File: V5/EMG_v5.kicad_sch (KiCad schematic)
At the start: 1 part, among them U501 DSTK22807_ESP32H2_SuperMini_M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

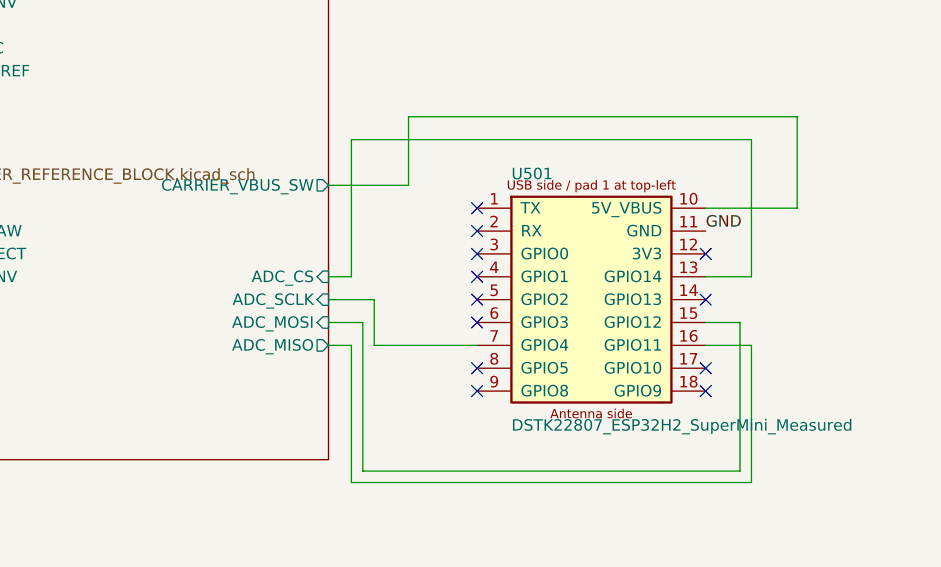
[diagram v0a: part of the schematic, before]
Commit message: add unequal-power spi isolation
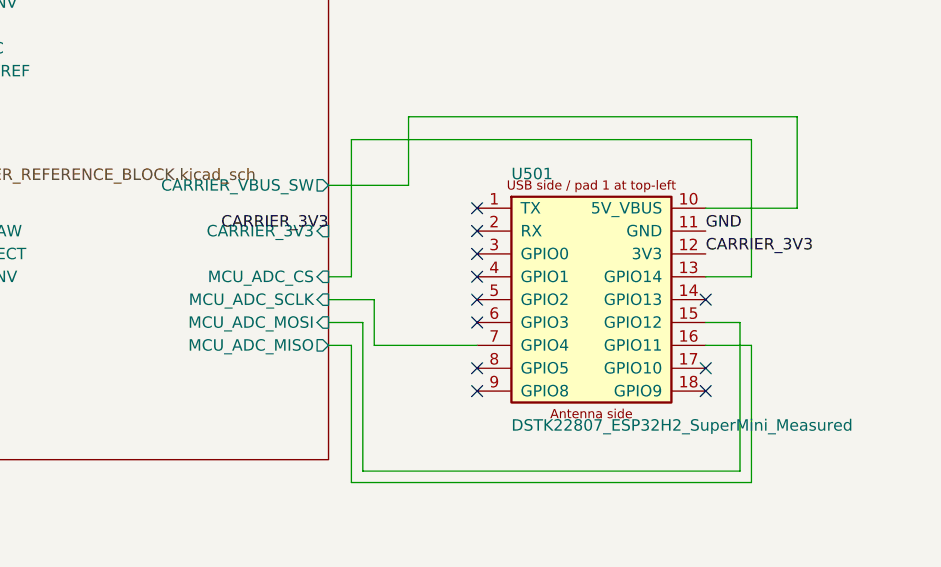
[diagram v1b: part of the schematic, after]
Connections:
- net CARRIER_3V3: now reaches U501.12 (3V3)
- net POWER_REFERENCE_BLOCK/ADC_CS renamed POWER_REFERENCE_BLOCK/MCU_ADC_CS
- net POWER_REFERENCE_BLOCK/ADC_MISO renamed POWER_REFERENCE_BLOCK/MCU_ADC_MISO
- net POWER_REFERENCE_BLOCK/ADC_MOSI renamed POWER_REFERENCE_BLOCK/MCU_ADC_MOSI
- net POWER_REFERENCE_BLOCK/ADC_SCLK renamed POWER_REFERENCE_BLOCK/MCU_ADC_SCLK
- no-connect marks 12 -> 11
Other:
- sheet POWER_REFERENCE_BLOCK ports: added CARRIER_3V3, MCU_ADC_CS, MCU_ADC_MISO, MCU_ADC_MOSI, MCU_ADC_SCLK; removed ADC_CS, ADC_MISO, ADC_MOSI, ADC_SCLK
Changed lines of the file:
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@@
 		(at 185.42 74.93)
 	)
-	(no_connect
-		(at 210.82 59.69)
+	(label "CARRIER_3V3"
+		(at 210.82 59.69 0)
+		(effects (font (size 1.27 1.27)) (justify left bottom))
+	)
+	(label "CARRIER_3V3"
+		(at 168.91 57.15 180)
+		(effects (font (size 1.27 1.27)) (justify right bottom))
 	)
 	(no_connect
@@
 			)
 		)
-		(pin "ADC_MISO" output
+		(pin "CARRIER_3V3" input
+			(at 168.91 57.15 0)
+			(effects (font (size 1.27 1.27)) (justify right))
+		)
+		(pin "MCU_ADC_MISO" output
 			(at 168.91 69.85 0)
 			(effects
@@
 			)
 		)
-		(pin "ADC_MOSI" input
+		(pin "MCU_ADC_MOSI" input
 			(at 168.91 67.31 0)
 			(effects
@@
 			)
 		)
-		(pin "ADC_SCLK" input
+		(pin "MCU_ADC_SCLK" input
 			(at 168.91 64.77 0)
 			(effects
@@
 			)
 		)
-		(pin "ADC_CS" input
+		(pin "MCU_ADC_CS" input
 			(at 168.91 62.23 0)
 			(effects

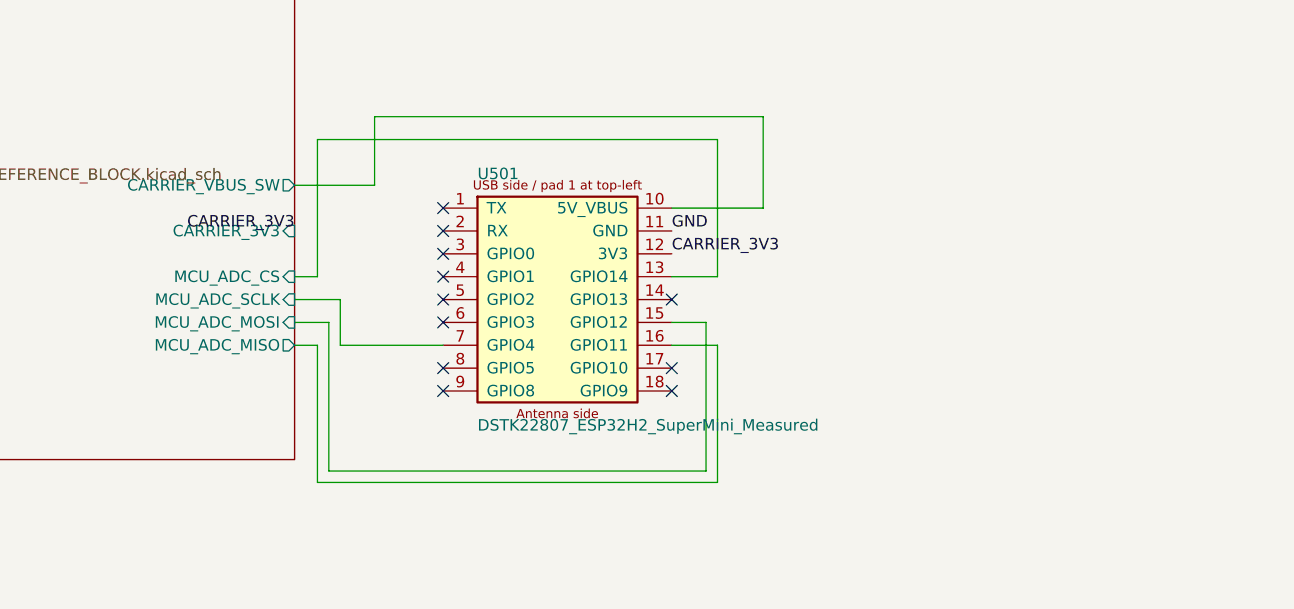
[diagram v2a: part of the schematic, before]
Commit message: Complete V5 PCB placement and debug access
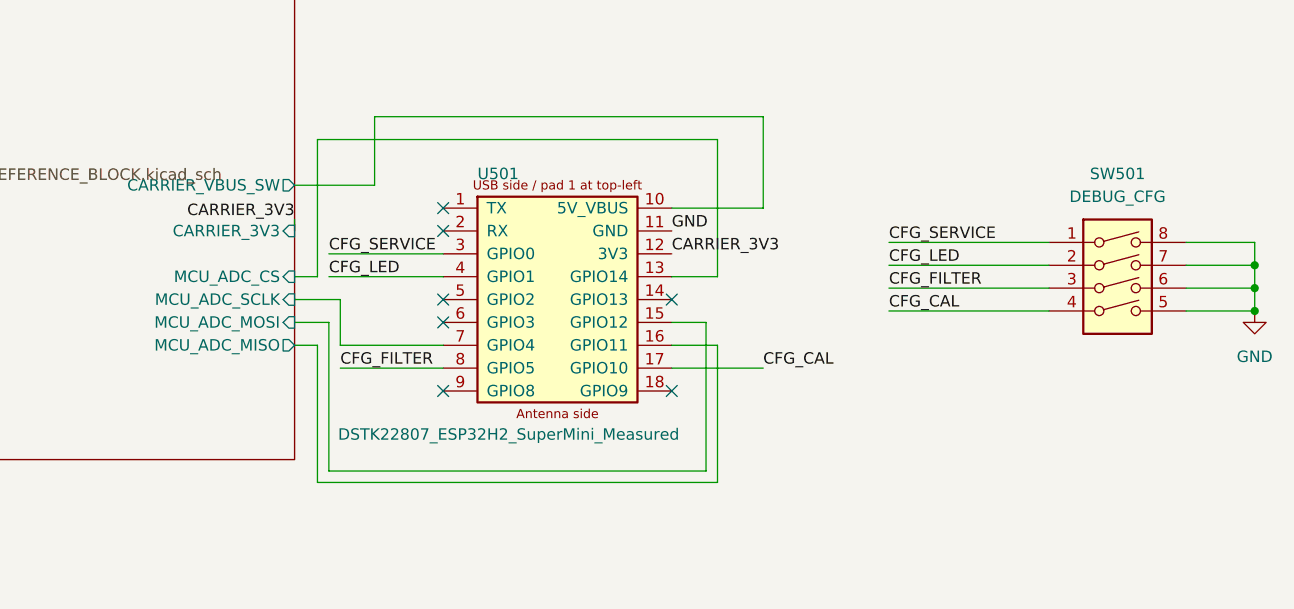
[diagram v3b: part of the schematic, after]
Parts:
- added SW501: DEBUG_CFG, Button_Switch_THT:SW_DIP_SPSTx04_Slide_9.78x12.34mm_W7.62mm_P2.54mm, symbol Switch:SW_DIP_x04
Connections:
- net GND: now also SW501.5, SW501.6, SW501.7, SW501.8
- net CFG_CAL: now reaches U501.17 (GPIO10)
- net CFG_CAL: now also SW501.4
- net CFG_SERVICE: now reaches U501.3 (GPIO0)
- net CFG_SERVICE: now also SW501.1
- net CFG_LED: now reaches U501.4 (GPIO1)
- net CFG_LED: now also SW501.2
- net CFG_FILTER: now reaches U501.8 (GPIO5)
- net CFG_FILTER: now also SW501.3
- no-connect marks 11 -> 7
